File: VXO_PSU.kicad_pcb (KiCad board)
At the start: 4 copper layers, 199.4 x 40.6 mm, 53 parts, among them CON1 BARREL_JACK, P1 CONN_01X02, P10 CONN_02X08, P12 BNC, P13 BNC, P2 CONN_02X08, P3 CONN_02X08, P4 CONN_02X08, P5 CONN_02X08, P6 CONN_02X08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

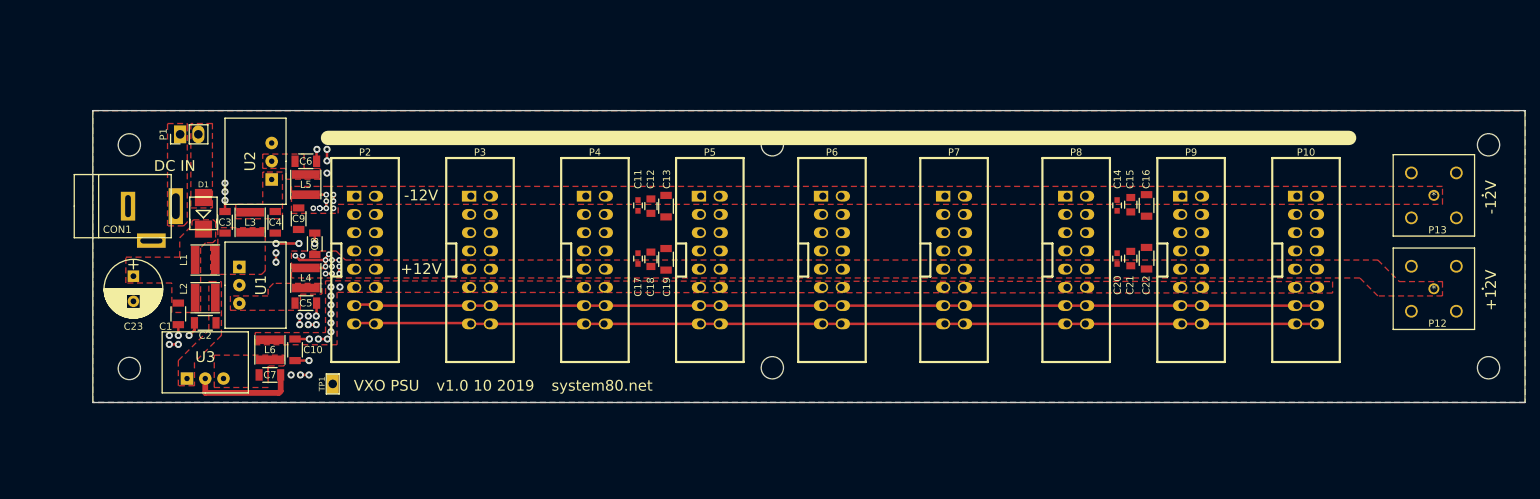
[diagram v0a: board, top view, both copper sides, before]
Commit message: rework to verson 1.1, changing inductors, removing pi output filters
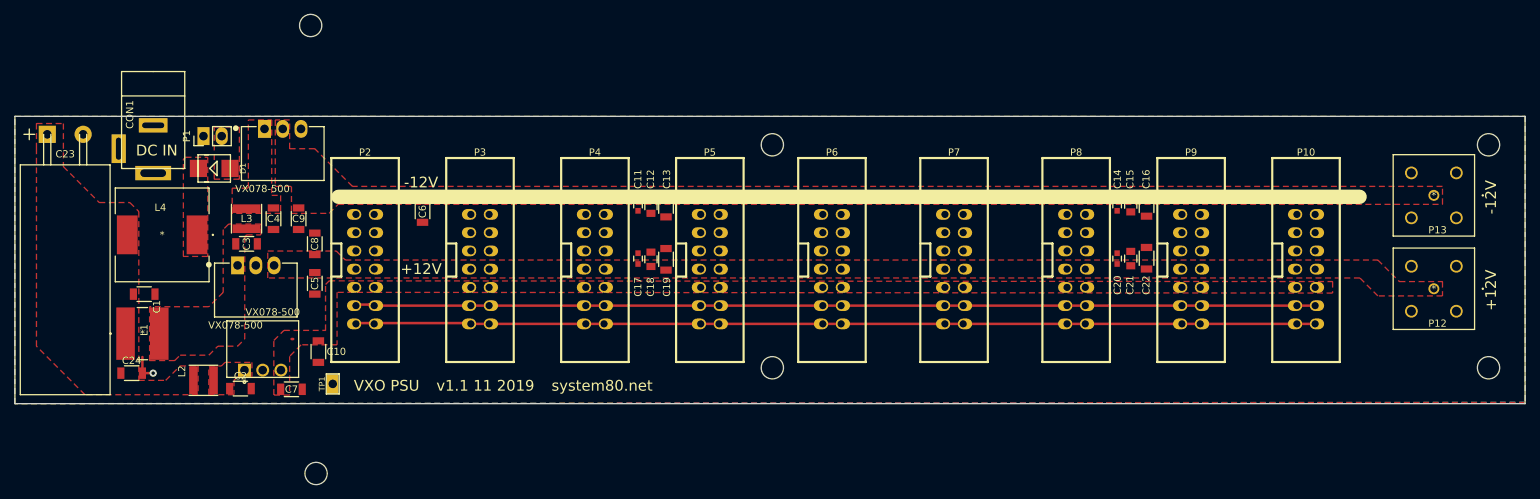
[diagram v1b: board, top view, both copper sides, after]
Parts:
- removed L5, L6: 10µH, Inductors_SMD:L_Taiyo-Yuden_NR-40xx
- added C24: 4.7µ, Capacitors_SMD:C_1206, F.Cu at (43.5, 112.8)
- C23: value CP_US -> 680µF; footprint Capacitors_THT:CP_Radial_D8.0mm_P3.50mm -> CP_Radial_D12.5mm_P5.00mm_reclined
- L1: footprint Inductors_SMD:L_Taiyo-Yuden_NR-40xx -> MyModules:SRR6038-120Y
- L4: value 10µH -> 82µH; footprint Inductors_SMD:L_Taiyo-Yuden_NR-40xx -> MyModules:SRR1260-820M
- U1, U2: footprint MyModules:R-78E-0.5 -> MyModules:CONV_VXO78012-1000
- U3: footprint MyModules:R-78E-0.5 -> MyModules:CUI_VXO780XX-500
- moved HOLE-M3 54.0 mm to (68.4, 64.3)
- moved HOLE-M3 52.6 mm to (69.2, 126.7)
- moved C23 23.1 mm to (31.8, 79.5), turned to 0 degrees
- moved L4 20.9 mm to (47.8, 93.5), turned to 180 degrees
- moved C6 17.7 mm to (84.0, 90.2), turned to 90 degrees
- moved L1 13.5 mm to (45.0, 107.2)
- moved L2 11.5 mm to (53.5, 113.8)
- moved C2 10.4 mm to (58.6, 114.9), turned to 0 degrees
- moved U3 10.2 mm to (61.8, 107.2), turned to 180 degrees
- moved CON1 8.00 mm to (46.5, 81.5), turned to 180 degrees
- moved D1 6.43 mm to (55.0, 84.2), turned to 0 degrees
- moved C1 5.49 mm to (45.2, 101.8), turned to 0 degrees
- moved U2 4.61 mm to (62.0, 78.8), turned to 0 degrees
- moved C3 4.24 mm to (59.5, 94.8), turned to 0 degrees
- moved C7 3.61 mm to (65.8, 115.0)
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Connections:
- C5 pad 1: Net-(C5-Pad1) -> +12V
- C6 pad 2: Net-(C6-Pad2) -> -12V
- C7 pad 1: Net-(C7-Pad1) -> +5V
- D1 pad 1: Net-(C1-Pad1) -> Net-(D1-Pad1)
- L4 pad 1: Net-(C5-Pad1) -> Net-(D1-Pad1)
- L4 pad 2: +12V -> Net-(C1-Pad1)
- U1 pad 3: Net-(C5-Pad1) -> +12V
- U2 pad 2: Net-(C6-Pad2) -> -12V
- U3 pad 3: Net-(C7-Pad1) -> +5V
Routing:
- net GND: track 57.3 -> 3.75 mm, vias 27 -> 1
- net +12V: track 18.0 -> 0.00 mm, vias 12 -> 0
- net +5V: track 13.2 -> 0.00 mm, vias 10 -> 0
- net -12V: track 9.55 -> 0.00 mm, vias 9 -> 0
- net (no net): track 1.20 -> 0.20 mm
- added copper zone on In1.Cu, net Net-(CON1-Pad1)
- added copper zone on F.Cu, net Net-(D1-Pad1)
- removed copper zone on F.Cu, net Net-(C5-Pad1)
- removed copper zone on F.Cu, net Net-(C6-Pad2)
- removed copper zone on F.Cu, net Net-(C7-Pad1)
- removed copper zone on F.Cu, net Net-(CON1-Pad1)
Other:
- board size 199.4 x 40.6 mm -> 210.2 x 40 mm
- board text added: "v1.1 11 2019"
- board text removed: "v1.0 10 2019"

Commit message: new 4 layer board updated, routed
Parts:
- P2: moved to B.Cu
- moved HOLE-M3 22.6 mm to (84.0, 80.7)
- moved HOLE-M3 20.9 mm to (84.1, 112.2)
- moved HOLE-M3 16.8 mm to (256.7, 112.0)
- moved HOLE-M3 16.8 mm to (149.5, 81.0)
- moved C7 0.11 mm to (65.8, 114.9)
- turned P2 to 90 degrees
